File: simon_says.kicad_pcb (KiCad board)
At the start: 2 copper layers, 97 x 60 mm, 24 parts, among them SW1 SW_Push_LED, SW2 SW_Push_LED, SW3 SW_Push_LED, SW4 SW_Push_LED, SW5 SW_Push, U1 ATtiny25-20P

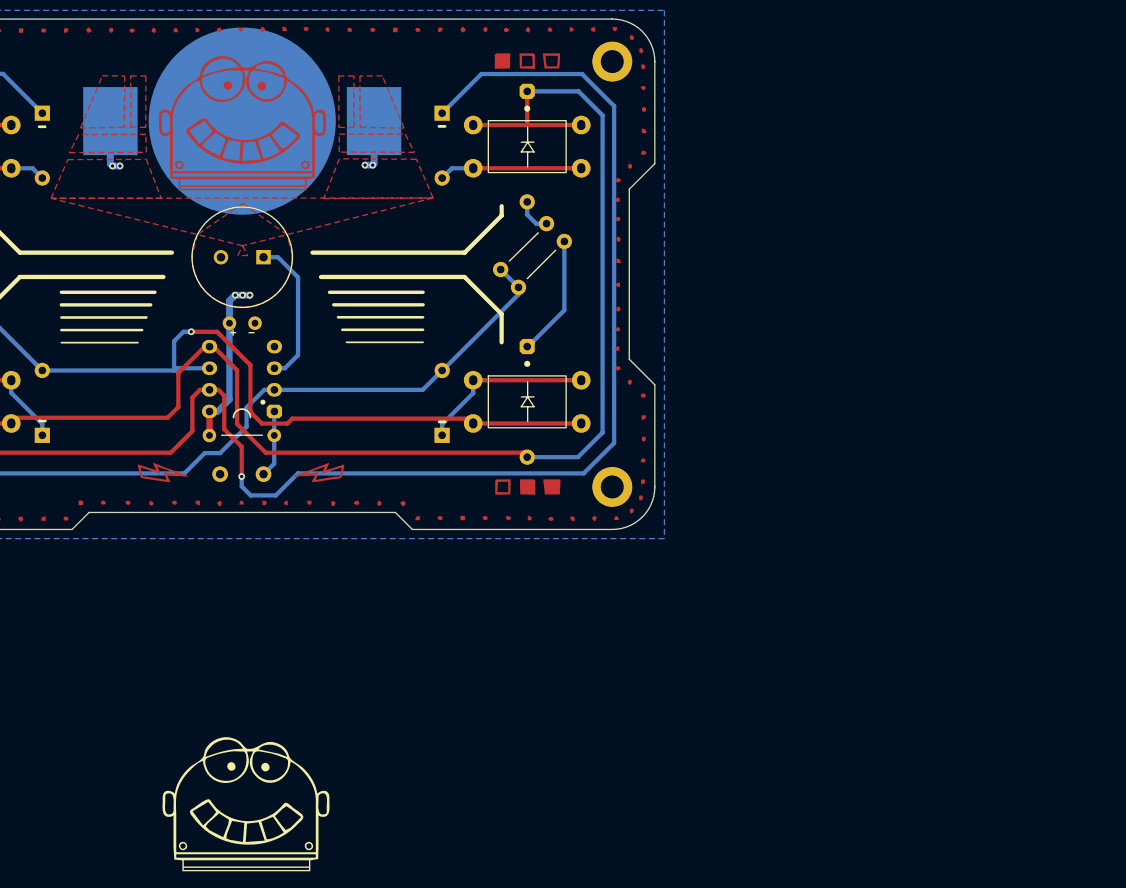
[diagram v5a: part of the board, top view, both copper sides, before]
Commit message: Updated graphic elements
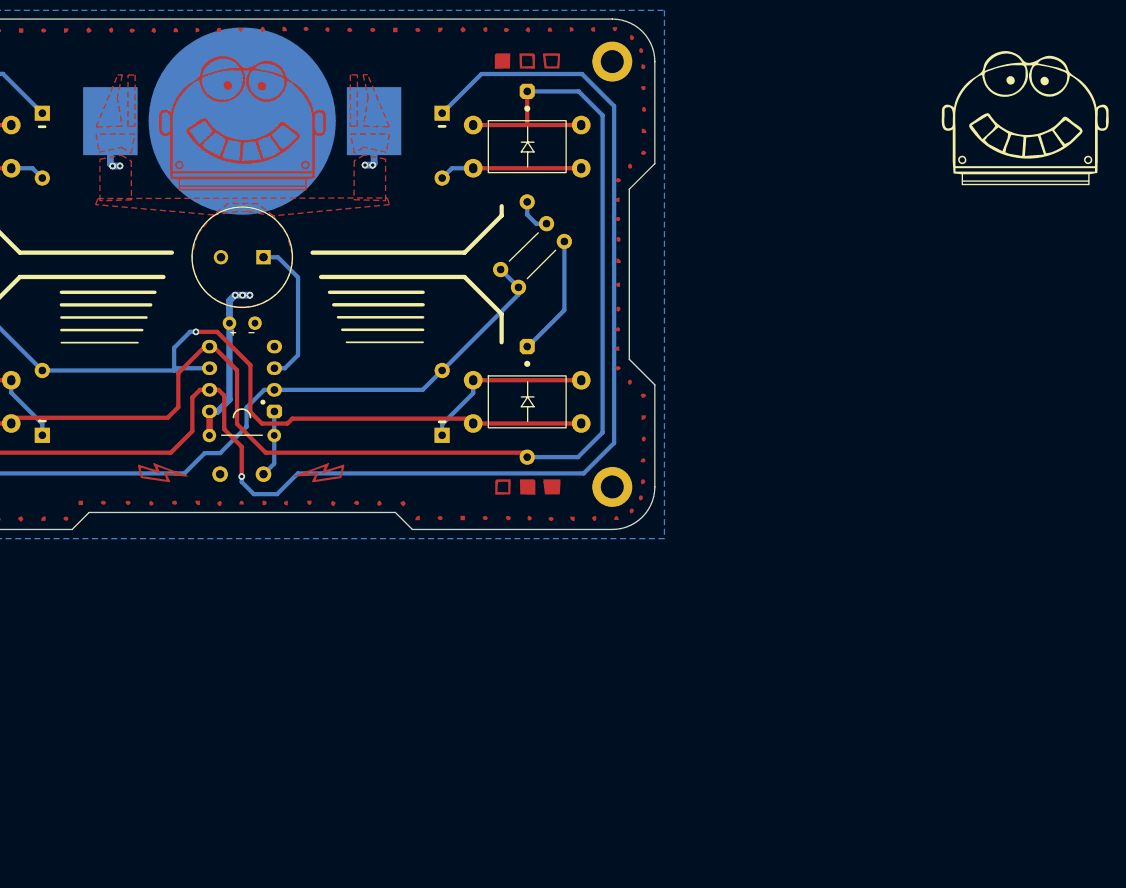
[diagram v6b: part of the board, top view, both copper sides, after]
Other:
- board text added: "rev1 0823"
- board text added: "rev2 0524"
